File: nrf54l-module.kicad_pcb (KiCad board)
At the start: 4 copper layers, 16 x 25 mm, 80 parts, among them SW1 TS24CA, U1 NRF54L15-QFAA-R, U2 XL-0201SURC, U3 TLV62569DBVR, U4 XL-0201SURC, U5 XL-0201SURC, X1 XL7EL89CKI-111YLC-32M

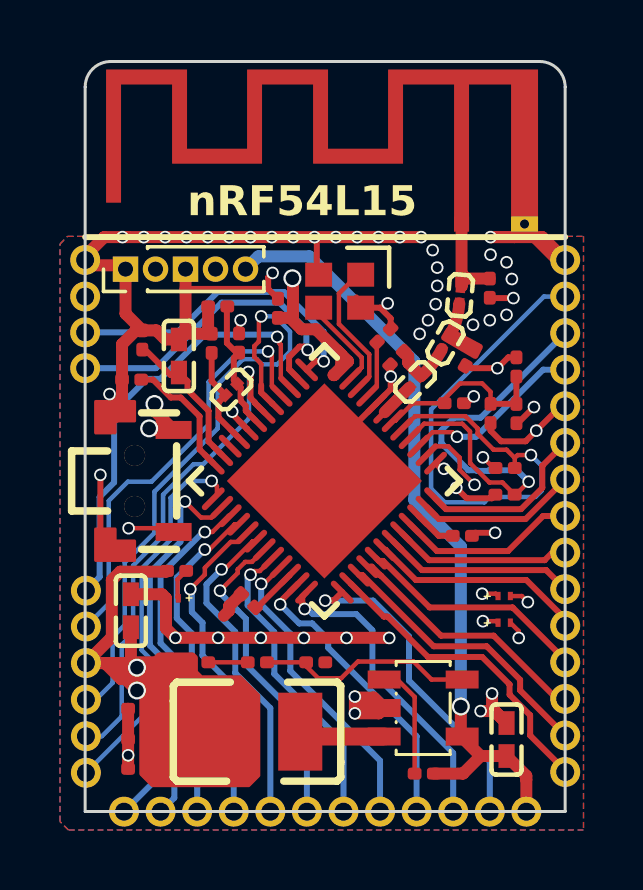
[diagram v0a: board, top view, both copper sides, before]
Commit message: feat: back silkscreen
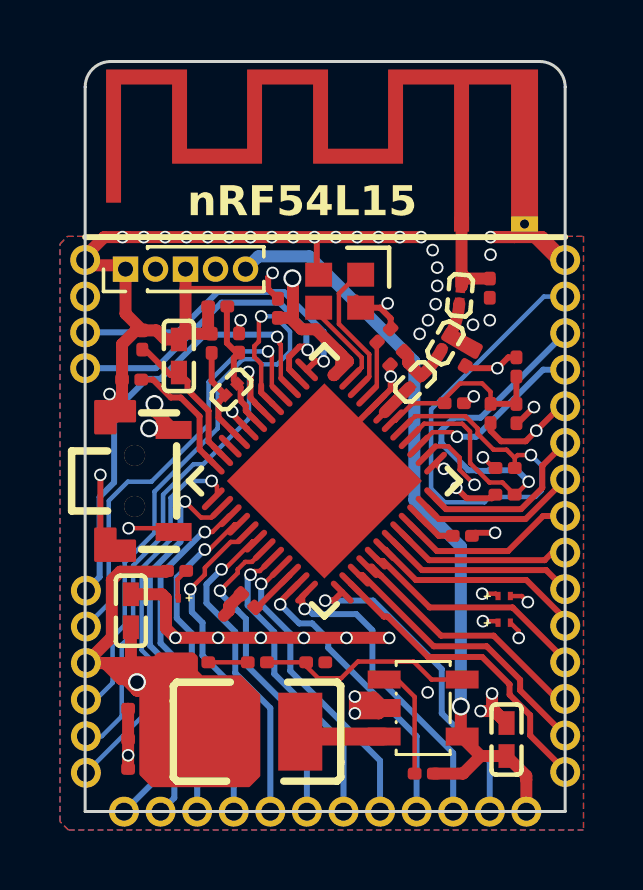
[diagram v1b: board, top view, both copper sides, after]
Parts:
- added kibuzzard-68448B88: G***, kibuzzard-68448B88, B.Cu at (50.5, 45.2)
- added kibuzzard-68448BA2: G***, kibuzzard-68448BA2, B.Cu at (50.5, 46.4)
- added kibuzzard-68448C4F: G***, kibuzzard-68448C4F, B.Cu at (50.5, 53.8)
- added kibuzzard-68448C52: G***, kibuzzard-68448C52, B.Cu at (50.5, 55.0)
- added kibuzzard-68448C5C: G***, kibuzzard-68448C5C, B.Cu at (49.9, 56.2)
- added kibuzzard-68448C64: G***, kibuzzard-68448C64, B.Cu at (50.5, 57.5)
- added kibuzzard-68448C67: G***, kibuzzard-68448C67, B.Cu at (50.5, 58.7)
- added kibuzzard-68448C78: G***, kibuzzard-68448C78, B.Cu at (50.5, 59.9)
- added kibuzzard-68448D45: G***, kibuzzard-68448D45, B.Cu at (63.0, 42.8)
- added kibuzzard-68448D82: G***, kibuzzard-68448D82, B.Cu at (62.5, 44.0)
- added kibuzzard-68448D96: G***, kibuzzard-68448D96, B.Cu at (62.5, 45.2)
- added kibuzzard-68448DA6: G***, kibuzzard-68448DA6, B.Cu at (62.5, 46.5)
- added kibuzzard-68448DC1: G***, kibuzzard-68448DC1, B.Cu at (63.1, 47.7)
- added kibuzzard-68448DE0: G***, kibuzzard-68448DE0, B.Cu at (62.5, 48.9)
- added kibuzzard-68448DE9: G***, kibuzzard-68448DE9, B.Cu at (62.5, 50.1)
- added kibuzzard-68448E11: G***, kibuzzard-68448E11, B.Cu at (62.5, 51.3)
- added kibuzzard-68448E3B: G***, kibuzzard-68448E3B, B.Cu at (62.5, 52.6)
- added kibuzzard-68448E4C: G***, kibuzzard-68448E4C, B.Cu at (62.5, 53.8)
- added kibuzzard-68448E55: G***, kibuzzard-68448E55, B.Cu at (62.5, 55.0)
- added kibuzzard-68448FBA: G***, kibuzzard-68448FBA, B.Cu at (51.8, 41.6)
- added kibuzzard-68448FBA: G***, kibuzzard-68448FBA, B.Cu at (49.8, 41.6)
- added kibuzzard-68448FEC: G***, kibuzzard-68448FEC, B.Cu at (50.8, 41.1)
- added kibuzzard-68449000: G***, kibuzzard-68449000, B.Cu at (50.6, 37.0)
- added kibuzzard-68449008: G***, kibuzzard-68449008, B.Cu at (51.8, 38.1)
- added kibuzzard-68449044: G***, kibuzzard-68449044, B.Cu at (52.8, 41.1)
- added kibuzzard-68449057: G***, kibuzzard-68449057, B.Cu at (53.8, 41.6)
- added kibuzzard-68449249: G***, kibuzzard-68449249, B.Cu at (62.3, 40.0)
- added kibuzzard-6844924F: G***, kibuzzard-6844924F, B.Cu at (61.1, 40.0)
- added kibuzzard-68449253: G***, kibuzzard-68449253, B.Cu at (63.6, 40.6)
- added kibuzzard-68449303: G***, kibuzzard-68449303, B.Cu at (53.4, 59.4)
- added kibuzzard-68449307: G***, kibuzzard-68449307, B.Cu at (54.6, 59.4)
- added kibuzzard-6844930A: G***, kibuzzard-6844930A, B.Cu at (55.9, 59.4)
- added kibuzzard-6844930F: G***, kibuzzard-6844930F, B.Cu at (57.1, 59.4)
- added kibuzzard-68449316: G***, kibuzzard-68449316, B.Cu at (58.3, 59.4)
- added kibuzzard-6844931D: G***, kibuzzard-6844931D, B.Cu at (59.5, 59.4)
- added kibuzzard-68449351: G***, kibuzzard-68449351, B.Cu at (56.1, 49.4)
- added kibuzzard-68449359: G***, kibuzzard-68449359, B.Cu at (53.6, 49.4)
- added kibuzzard-68449360: G***, kibuzzard-68449360, B.Cu at (54.9, 49.4)
- added kibuzzard-684495B0: G***, kibuzzard-684495B0, B.Cu at (62.5, 56.2)
- added kibuzzard-684495B4: G***, kibuzzard-684495B4, B.Cu at (62.5, 57.4)
- added kibuzzard-684495B8: G***, kibuzzard-684495B8, B.Cu at (62.5, 58.6)
- added kibuzzard-684495BB: G***, kibuzzard-684495BB, B.Cu at (62.5, 59.9)
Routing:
- net GND: track 70.6 -> 69.9 mm, vias 51 -> 48
- net +1V8: track 52.0 -> 51.3 mm, vias 5 -> 4
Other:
- board text added: "RESET"
- board text added: "VIN: 1.8-5.5V"

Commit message: bugfix: GND pad
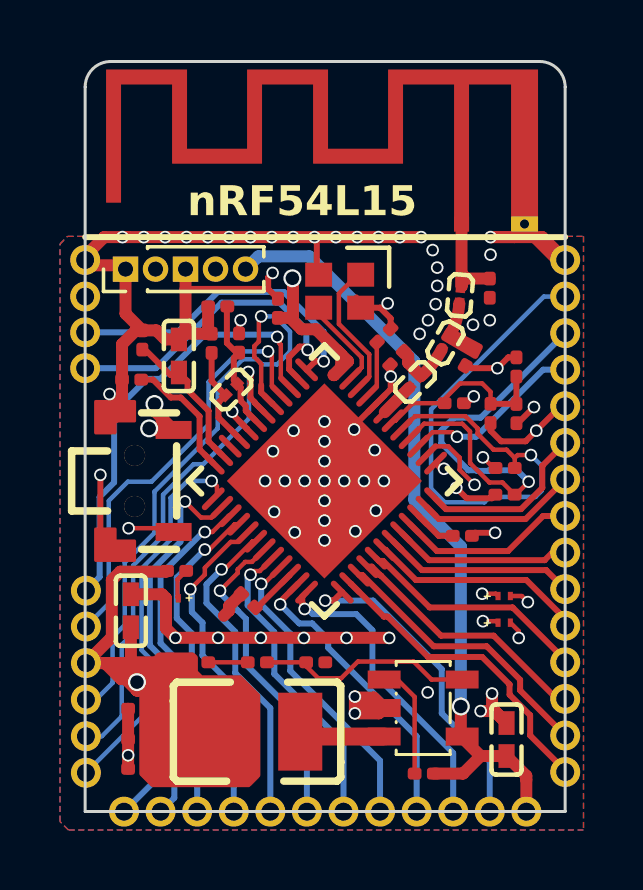
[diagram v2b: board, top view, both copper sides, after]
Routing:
- net GND: vias 48 -> 69

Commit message: chore: refactoring
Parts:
- L4: value 2.2uF -> 2.2uH
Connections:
- AE1 pad 2: GND -> (no net)
- SW1 pad 2: GND -> (no net)
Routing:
- net GND: track 69.9 -> 69.3 mm, vias 69 -> 67

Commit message: chore: refactoring
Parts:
- removed kibuzzard-68448FEC: G***, kibuzzard-68448FEC
- removed kibuzzard-68449044: G***, kibuzzard-68449044
- added kibuzzard-6844ABB3: G***, kibuzzard-6844ABB3, B.Cu at (52.8, 41.6)
- added kibuzzard-6844ABB6: G***, kibuzzard-6844ABB6, B.Cu at (50.8, 41.6)
- moved kibuzzard-68449249 15.3 mm to (57.8, 54.6)
- moved kibuzzard-6844924F 15.3 mm to (56.5, 54.6)
- moved kibuzzard-68449253 15.3 mm to (59.0, 55.1)
- moved kibuzzard-68449359 1.17 mm to (54.5, 50.1)
- moved kibuzzard-68449360 1.17 mm to (55.7, 50.1)
- moved kibuzzard-68449351 1.17 mm to (57.0, 50.1)
- moved kibuzzard-68449008 0.28 mm to (51.8, 38.3)
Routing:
- net GND: track 69.3 -> 59.7 mm

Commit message: chore: refactoring
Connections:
- AE1 pad 2: (no net) -> GND
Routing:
- net GND: track 59.7 -> 45.9 mm, vias 67 -> 65
- net SWDIO: track 11.1 -> 12.1 mm
- net SWDCLK: track 17.7 -> 17.1 mm

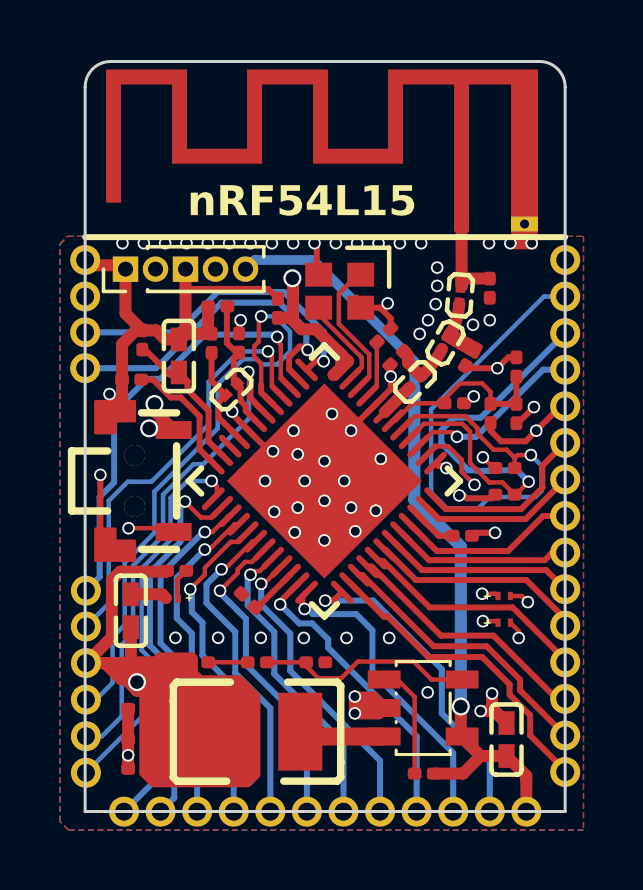
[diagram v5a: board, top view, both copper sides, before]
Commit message: bugfix: antenna design
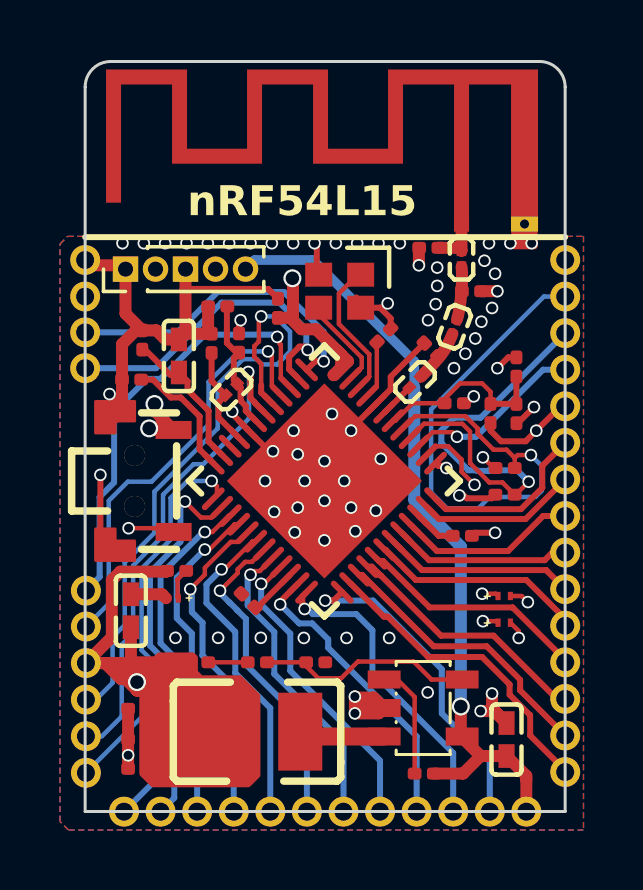
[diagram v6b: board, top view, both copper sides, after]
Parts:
- moved C7 2.44 mm to (59.9, 42.4), turned to 180 degrees
- moved C8 2.21 mm to (61.4, 43.8), turned to 0 degrees
- moved L3 1.22 mm to (61.0, 42.8), turned to -90 degrees
- moved C6 1.18 mm to (60.0, 45.8), turned to 135 degrees
- moved L2 0.61 mm to (60.8, 45.0), turned to -110 degrees
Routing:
- net Net-(AE1-A): track 3.41 -> 1.70 mm
- net GND: track 45.9 -> 47.0 mm, vias 65 -> 69
- net Net-(C6-Pad1): track 1.06 -> 0.00 mm
